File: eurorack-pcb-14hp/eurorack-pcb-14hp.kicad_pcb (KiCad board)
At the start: 2 copper layers, 18.5 x 108.3 mm, 0 parts

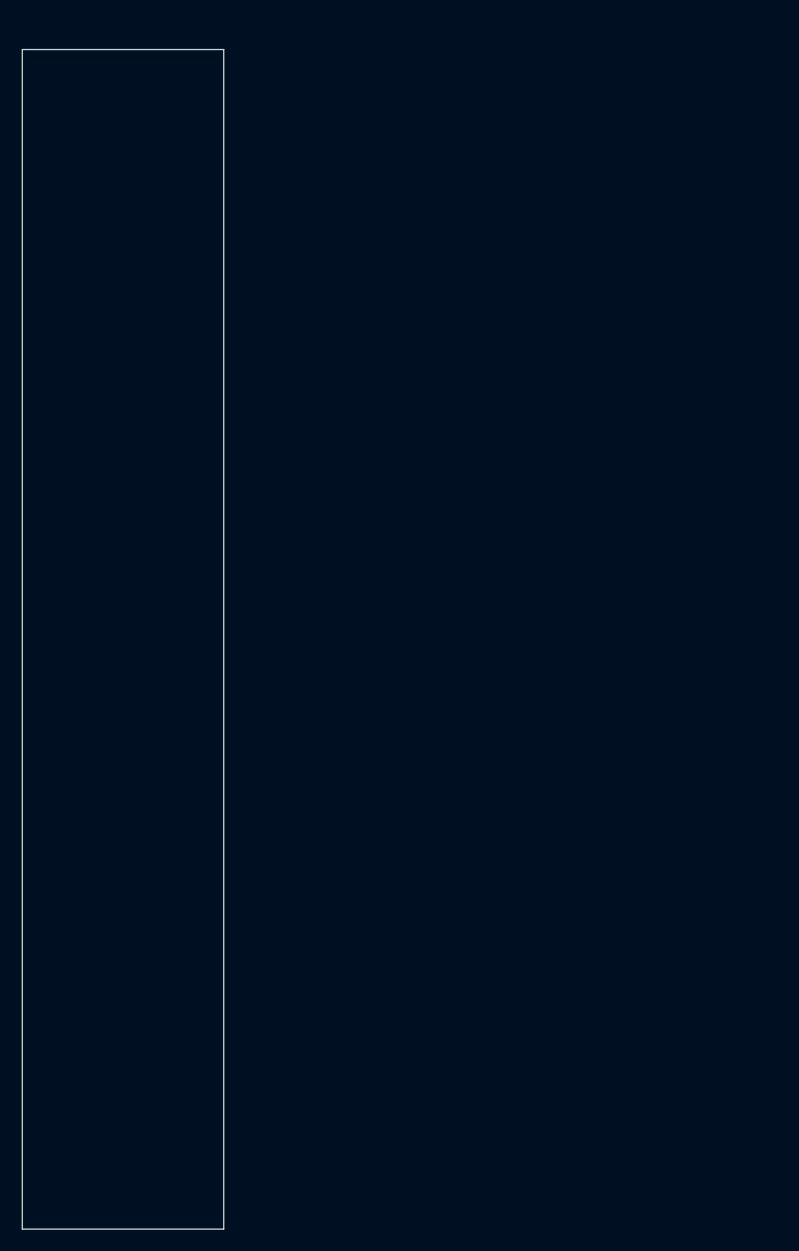
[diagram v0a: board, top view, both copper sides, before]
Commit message: Minor adjustments to PCB positioning. Moving everything into a single folder to be easier for kiCad to pick up all templates from user-template path
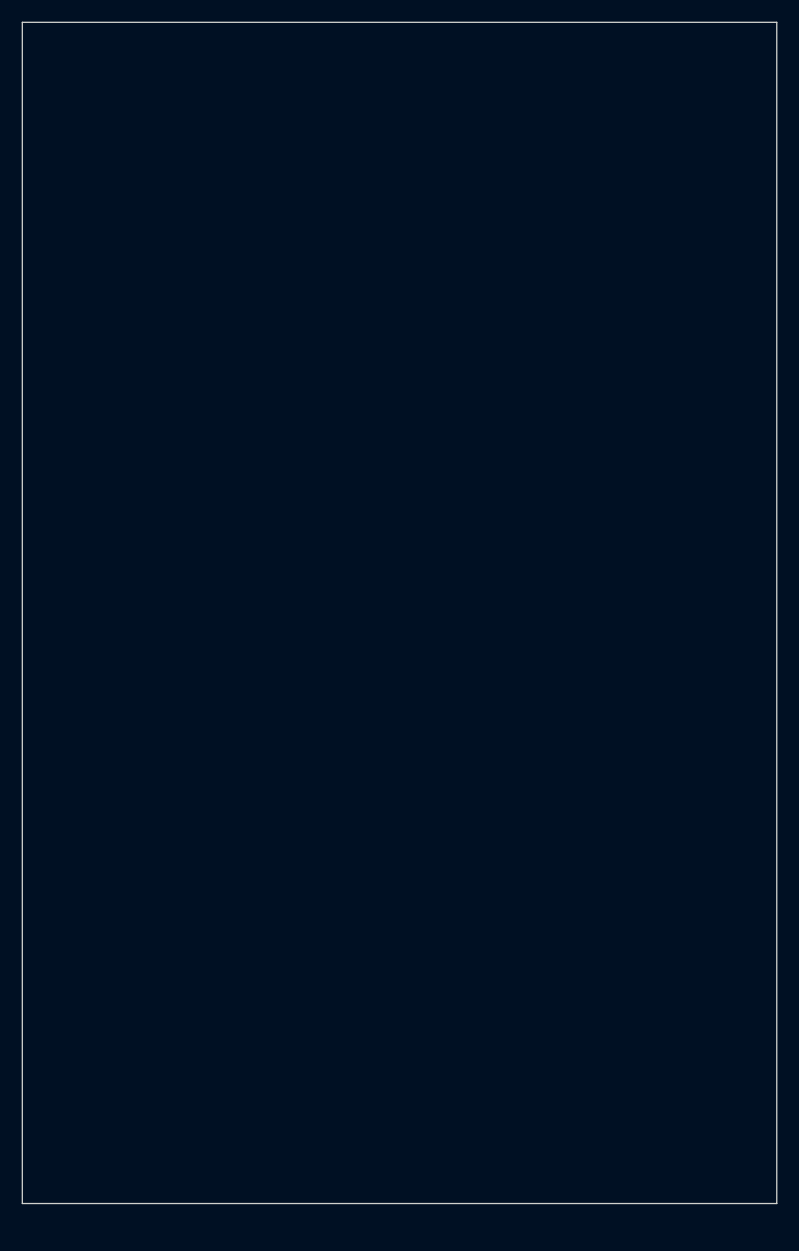
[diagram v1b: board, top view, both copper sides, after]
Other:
- board size 18.5 x 108.3 mm -> 69.3 x 108.5 mm
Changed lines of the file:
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@@
   )
   (net 0 "")
-  (gr_line (start 0.75 12.5) (end 0.75 120.85) (layer "Edge.Cuts") (width 0.1))
-  (gr_line (start 19.25 120.85) (end 19.25 12.5) (layer "Edge.Cuts") (width 0.1))
-  (gr_line (start 0.75 120.85) (end 19.25 120.85) (layer "Edge.Cuts") (width 0.1))
-  (gr_line (start 0.75 12.5) (end 19.25 12.5) (layer "Edge.Cuts") (width 0.1))
-  (gr_line (start 20 0) (end 20 128.5) (layer "User.1") (width 0.1))
+  (gr_line (start 0.75 10) (end 0.75 118.5) (layer "Edge.Cuts") (width 0.1))
+  (gr_line (start 70.05 118.5) (end 70.05 10) (layer "Edge.Cuts") (width 0.1))
+  (gr_line (start 0.75 118.5) (end 70.05 118.5) (layer "Edge.Cuts") (width 0.1))
+  (gr_line (start 0.75 10) (end 70.05 10) (layer "Edge.Cuts") (width 0.1))
+  (gr_line (start 70.8 0) (end 70.8 128.5) (layer "User.1") (width 0.1))
   (gr_line (start 0 128.5) (end 0 0) (layer "User.1") (width 0.1))
-  (gr_line (start 0 0) (end 20 0) (layer "User.1") (width 0.1))
-  (gr_line (start 20 128.5) (end 0 128.5) (layer "User.1") (width 0.1))
-  (dimension (type aligned) (layer "User.1")
-    (pts (xy 0.75 12.5) (xy 19.25 12.5))
-    (height -16.5)
-    (gr_text "18.5000 mm" (at 10 -5.15) (layer "User.1")
-      (effects (font (size 1 1) (thickness 0.15)))
-    )
-    (format (units 3) (units_format 1) (precision 4))
-    (style (thickness 0.1) (arrow_length 1.27) (text_position_mode 0) (extension_height 0.58642) (extension_offset 0.5) keep_text_aligned)
-  )
-  (dimension (type aligned) (layer "User.1")
-    (pts (xy 19.25 120.85) (xy 19.25 12.5))
-    (height 4.75)
-    (gr_text "108.3500 mm" (at 22.85 66.675 90) (layer "User.1")
-      (effects (font (size 1 1) (thickness 0.15)))
-    )
-    (format (units 3) (units_format 1) (precision 4))
-    (style (thickness 0.1) (arrow_length 1.27) (text_position_mode 0) (extension_height 0.58642) (extension_offset 0.5) keep_text_aligned)
-  )
+  (gr_line (start 0 0) (end 70.8 0) (layer "User.1") (width 0.1))
+  (gr_line (start 70.8 128.5) (end 0 128.5) (layer "User.1") (width 0.1))
 )
